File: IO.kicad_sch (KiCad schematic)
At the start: 2 parts, among them J1 USB-C-(USB4056-03-A_REVA2)

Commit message: Connexion partielle du connecteur usb
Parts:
- removed J1: USB-C-(USB4056-03-A_REVA2), USB4056-03-A_REVA2:GCT_USB4056-03-A_REVA2, symbol GAUL-Symboles:USB-C-(USB4056-03-A_REVA2)
- added J1: conn_USB-A-(UE27AC54100), UE27AC54100:AMPHENOL_UE27AC54100, symbol GAUL-Symboles:conn_USB-A-(UE27AC54100)
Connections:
- net GND: now also J1.4 (GND), J1.S1 (SHIELD), J1.S2 (SHIELD__1)
- net Vusb: now also J1.1 (VCC)
- new net USB_D+: J1.3 (D+)
- new net USB_D-: J1.2 (D-)

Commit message: Mémoire
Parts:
- added U15, U5: AS5F32G04SNDA-08LIN(mémoire), IC8_AS5F12G04SND-10LIN_ALL, symbol GAUL-Symboles:AS5F32G04SNDA-08LIN(mémoire)
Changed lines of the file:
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@@
+    )
+  )
+  (symbol (lib_id "GAUL-Symboles:AS5F32G04SNDA-08LIN(mémoire)") (at 158.75 146.05 0) (unit 1)
+    (in_bom yes) (on_board yes) (dnp no) (fields_autoplaced)
+    (property "Reference" "U15" (at 189.23 135.89 0)
+      (effects (font (size 1.524 1.524)))
+    )
+    (property "Value" "AS5F32G04SNDA-08LIN(mémoire)" (at 189.23 138.43 0)
+      (effects (font (size 1.524 1.524)))
+    )
+    (property "Footprint" "IC8_AS5F12G04SND-10LIN_ALL" (at 158.75 146.05 0)
+      (effects (font (size 1.27 1.27) italic) hide)
+    )
+    (property "Datasheet" "AS5F12G04SND-10LIN" (at 158.75 146.05 0)
+      (effects (font (size 1.27 1.27) italic) hide)
+    )
+    (pin "4")
+    (pin "8")
+    (pin "7")
+    (pin "5")
+    (pin "2")
+    (pin "3")
+    (pin "6")
+    (pin "1")
+    (instances
+      (project "Payload"
+        (path "/5f62c44b-34ee-4720-b187-b4a520863a8a/5a04916d-02c4-4327-b1de-b8c4998ffa12"
+          (reference "U15") (unit 1)
+        )
+      )
     )
   )
@@
         )
       )
+    )
+  )
+  (symbol (lib_id "GAUL-Symboles:AS5F32G04SNDA-08LIN(mémoire)") (at 82.55 146.05 0) (unit 1)
+    (in_bom yes) (on_board yes) (dnp no) (fields_autoplaced)
+    (property "Reference" "U5" (at 113.03 135.89 0)
+      (effects (font (size 1.524 1.524)))
+    )
+    (property "Value" "AS5F32G04SNDA-08LIN(mémoire)" (at 113.03 138.43 0)
+      (effects (font (size 1.524 1.524)))
+    )
+    (property "Footprint" "IC8_AS5F12G04SND-10LIN_ALL" (at 82.55 146.05 0)
+      (effects (font (size 1.27 1.27) italic) hide)
+    )
+    (property "Datasheet" "AS5F12G04SND-10LIN" (at 82.55 146.05 0)
+      (effects (font (size 1.27 1.27) italic) hide)
+    )
+    (pin "4")
+    (pin "8")
+    (pin "7")
+    (pin "5")
+    (pin "2")
+    (pin "3")
+    (pin "6")
+    (pin "1")
+    (instances
+      (project "Payload"
+        (path "/5f62c44b-34ee-4720-b187-b4a520863a8a/5a04916d-02c4-4327-b1de-b8c4998ffa12"
+          (reference "U5") (unit 1)
+        )
+      )

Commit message: Schematic fini, en théorie
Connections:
- net +3.3V: now also U15.8 (VCC), U5.8 (VCC)
- net GND: now also U15.4 (VSS), U5.4 (VSS)
- net QUADSPI_BK1_NCS: now reaches U15.1 (CS#)
- net QUADSPI_BK1_IO3: now reaches U15.2 (SO/SIO1)
- net QUADSPI_BK1_IO2: now reaches U15.3 (WP#/SIO2)
- net QUADSPI_BK1_IO0: now reaches U15.5 (SI/SIO0)
- net QUADSPI_CLK: now reaches U15.6 (SCLK)
- net QUADSPI_CLK: now also U5.6 (SCLK)
- net QUADSPI_BK1_IO1: now reaches U15.7 (HOLD#/SIO3)
- net QUADSPI_BK2_NCS: now reaches U5.1 (CS#)
- net QUADSPI_BK2_IO1: now reaches U5.2 (SO/SIO1)
- net QUADSPI_BK2_IO2: now reaches U5.3 (WP#/SIO2)
- net QUADSPI_BK2_IO0: now reaches U5.5 (SI/SIO0)
- net QUADSPI_BK2_IO3: now reaches U5.7 (HOLD#/SIO3)
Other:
- note added: "Connecteur USB-A"
- note added: "Pins SWD pour prog"
- moved on the sheet: U15, U5

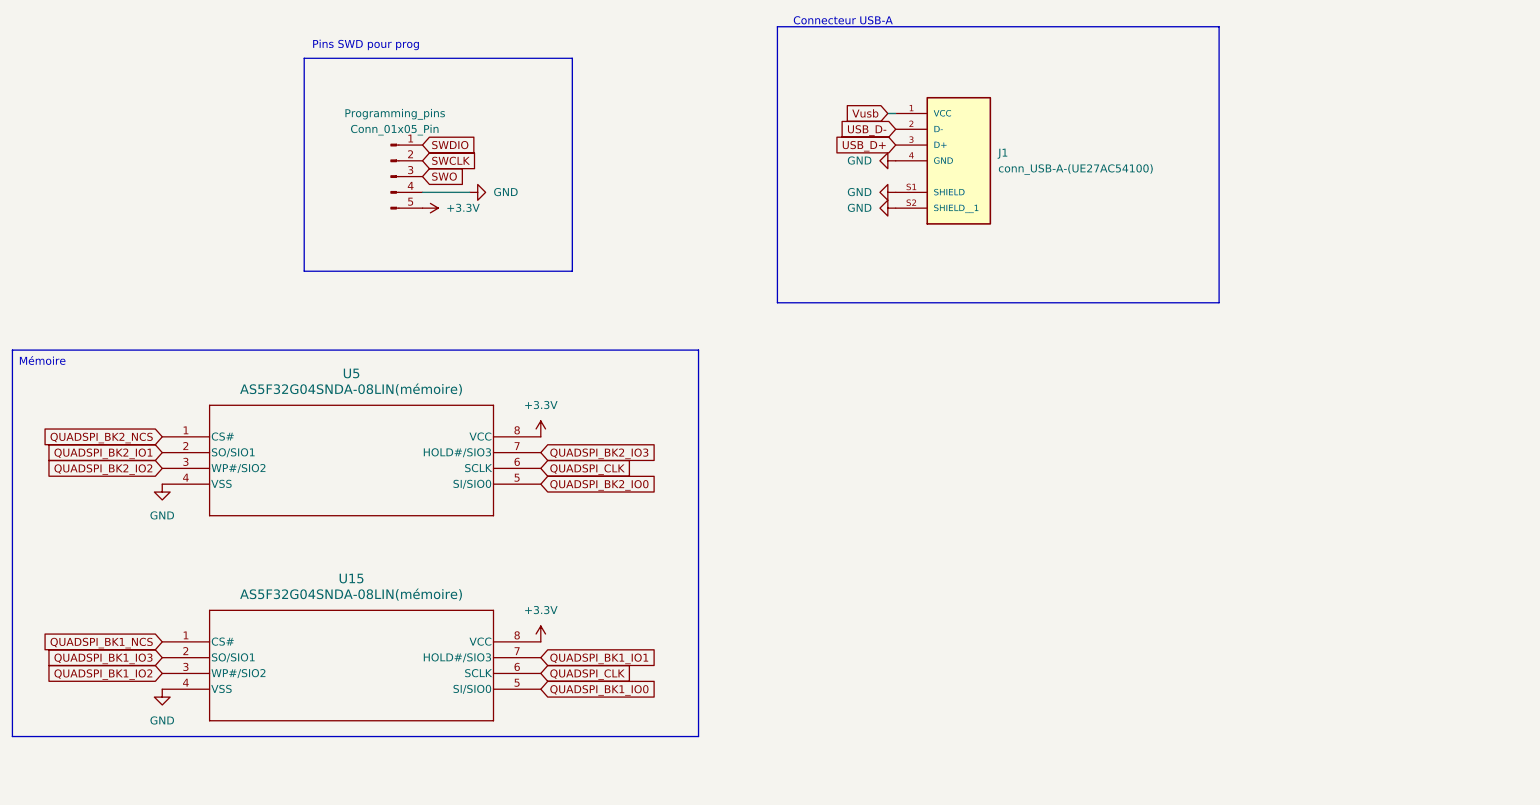
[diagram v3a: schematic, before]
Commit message: Petites modif et assignation des empreintes à 50%
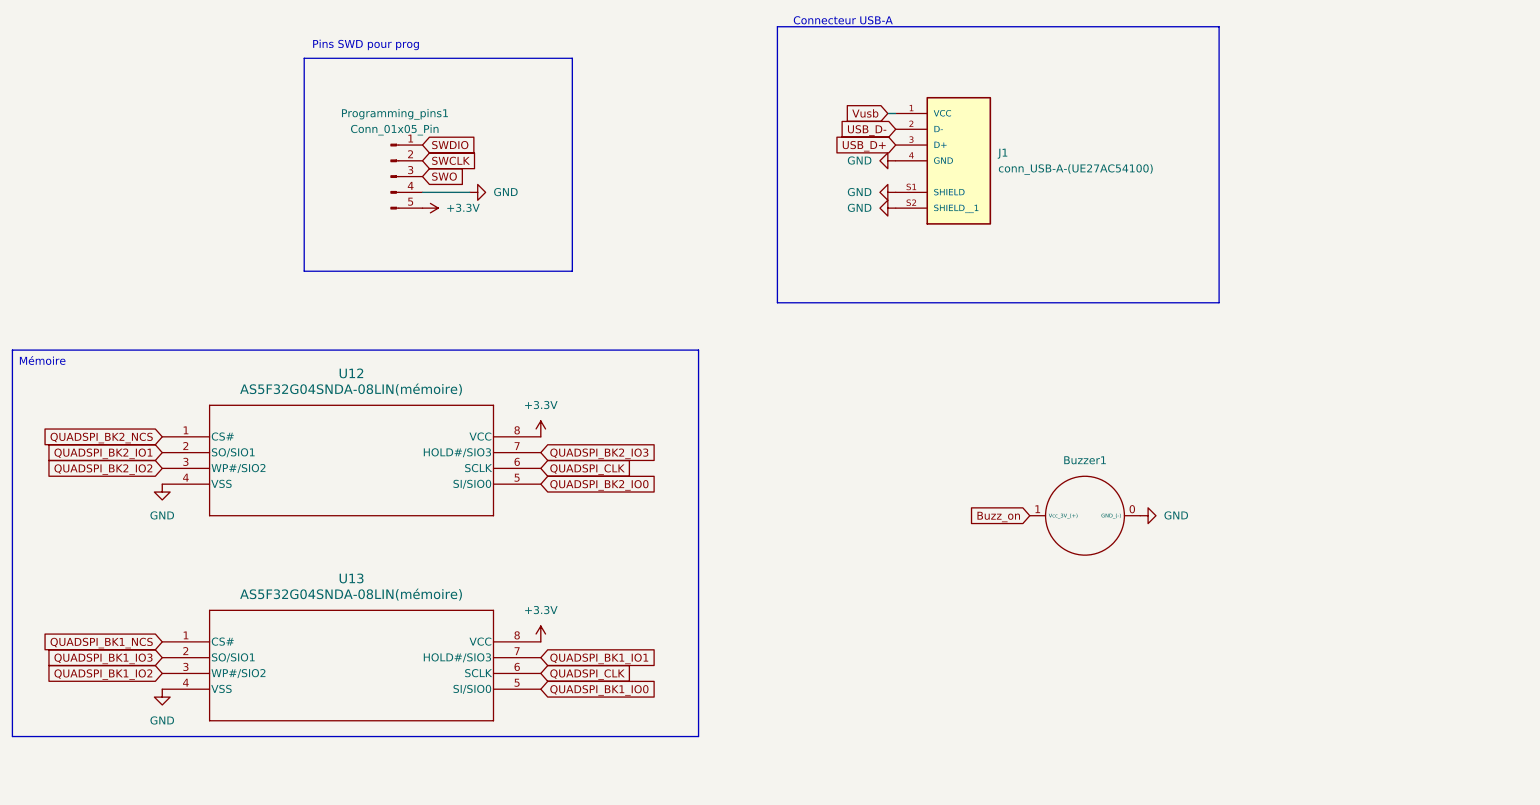
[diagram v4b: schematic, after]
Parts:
- added Buzzer1: ~, symbol GAUL-Symboles:Buzzer-(2104-IE092503-1-ND)
- U12: renamed from U5; footprint IC8_AS5F12G04SND-10LIN_ALL -> GAUL-Empreintes:IC8_AS5F12G04SND-10LIN_ALL-L
- U13: renamed from U15; footprint IC8_AS5F12G04SND-10LIN_ALL -> GAUL-Empreintes:IC8_AS5F12G04SND-10LIN_ALL-L
- renumbered Programming_pins to Programming_pins1
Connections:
- net GND: now also Buzzer1.0 (GND_(-))
- new net Buzz_on: Buzzer1.1 (Vcc_3V_(+))

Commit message: Début PCB
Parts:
- added U14: conn-fem-90deg-(PPPC062LJBN-RC), GAUL-Empreintes:conn-90deg-(CONN_PPPC062LJBN-RC_SUL), symbol GAUL-Symboles:conn-fem-90deg-(PPPC062LJBN-RC)
- Buzzer1: footprint (none) -> GAUL-Empreintes:buzzer-(IE092503-1)
- J1: footprint UE27AC54100:AMPHENOL_UE27AC54100 -> GAUL-Empreintes:conn-usbA-(AMPHENOL_UE27AC54100)
- Programming_pins1: footprint (none) -> GAUL-Empreintes:conn-swd5pin-(CONN5_1LFBN-RC_SUL)
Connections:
- net GND: now also U14.10, U14.11, U14.12, U14.7, U14.8, U14.9
- new net SG1_2: U14.1
- new net SG3_4: U14.2
- new net SG5_6: U14.3
- new net Therm1: U14.4
- new net Therm2: U14.5
- new net Vibro1: U14.6
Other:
- moved on the sheet: Buzzer1
